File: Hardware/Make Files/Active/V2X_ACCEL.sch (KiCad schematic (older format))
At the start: 4 parts, among them U19 ADXL345

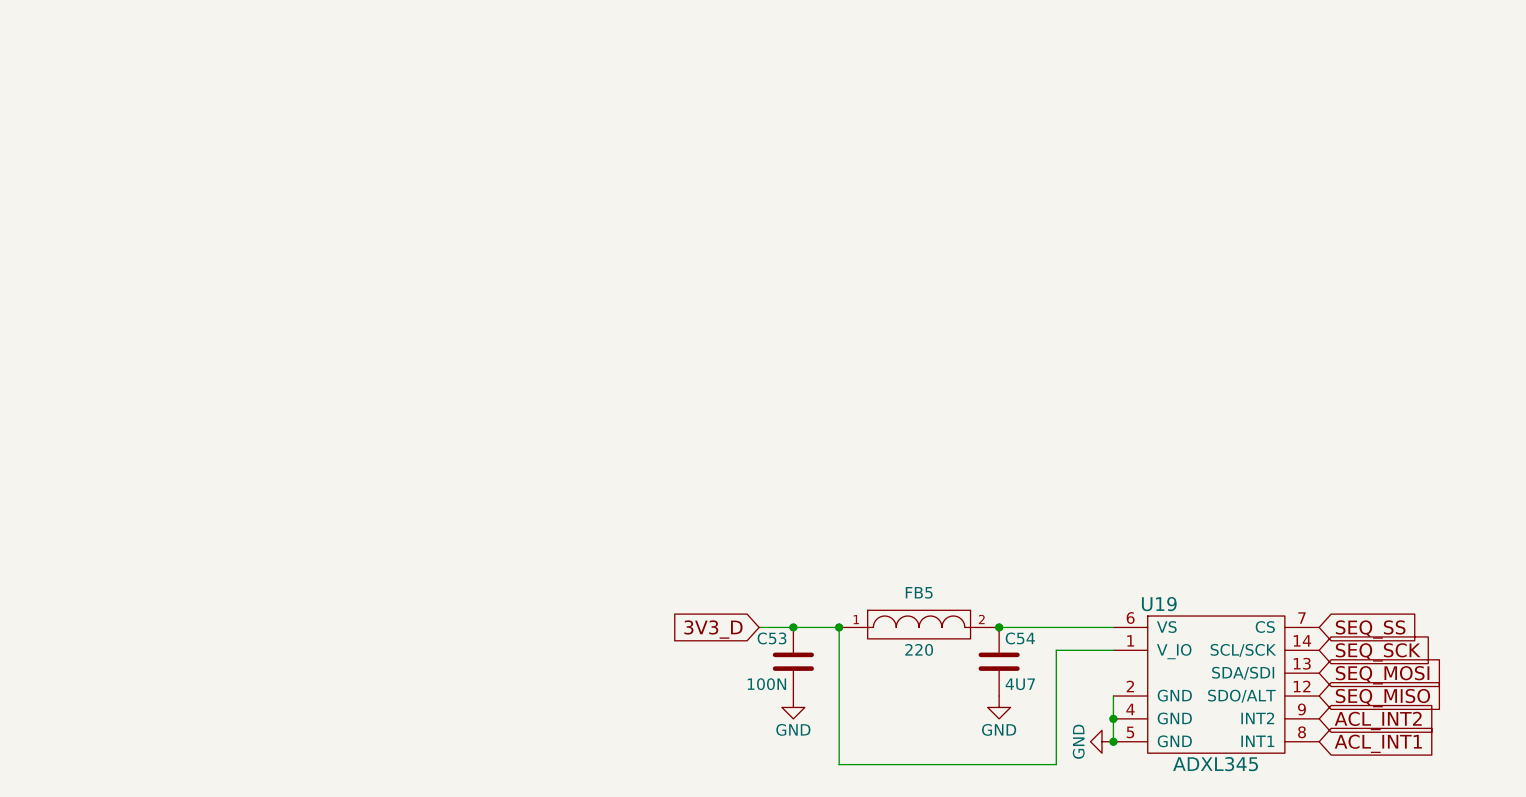
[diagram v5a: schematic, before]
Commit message: Project rework
Split the Main and GSM boards into separate projects, redesigned Main
board after flaws were found.
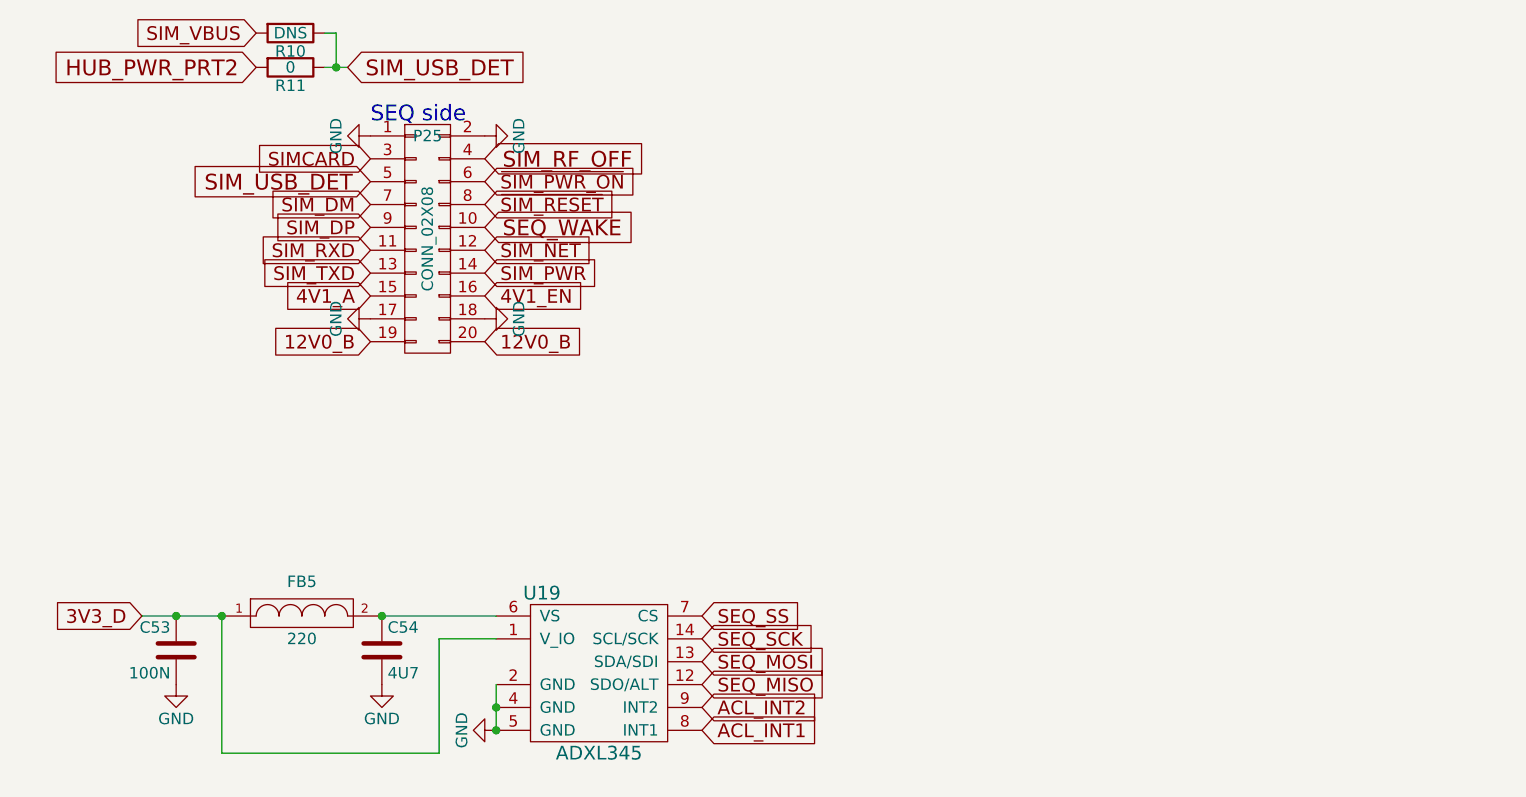
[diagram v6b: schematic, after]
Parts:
- added P25: CONN_02X08, Pin_Headers:Pin_Header_Straight_2x10, symbol CONN_02X10
- added R10: DNS, Custom Parts:R_0603_sm, symbol R
- added R11: 0, Custom Parts:R_0603_sm, symbol R
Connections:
- net GND: now also P25.1 (P1), P25.17 (P17), P25.18 (P18), P25.2 (P2)
- new net 12V0_B: P25.19 (P19), P25.20 (P20)
- new net 4V1_A: P25.15 (P15)
- new net 4V1_EN: P25.16 (P16)
- new net HUB_PWR_PRT2: R11.2
- new net SEQ_WAKE: P25.10 (P10)
- new net SIMCARD: P25.3 (P3)
- new net SIM_DM: P25.7 (P7)
- new net SIM_DP: P25.9 (P9)
- new net SIM_NET: P25.12 (P12)
- new net SIM_PWR: P25.14 (P14)
- new net SIM_RF_OFF: P25.4 (P4)
- new net SIM_RXD: P25.11 (P11)
- new net SIM_TXD: P25.13 (P13)
- new net SIM_USB_DET: P25.5 (P5), R10.1, R11.1
- new net SIM_VBUS: R10.2
- new net ~SIM_PWR_ON: P25.6 (P6)
- new net ~SIM_RESET: P25.8 (P8)
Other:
- note added: "SEQ side"
- moved on the sheet: C53, C54, FB5, U19
